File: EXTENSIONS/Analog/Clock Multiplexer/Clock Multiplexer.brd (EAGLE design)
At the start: 68 x 71 mm, 17 parts

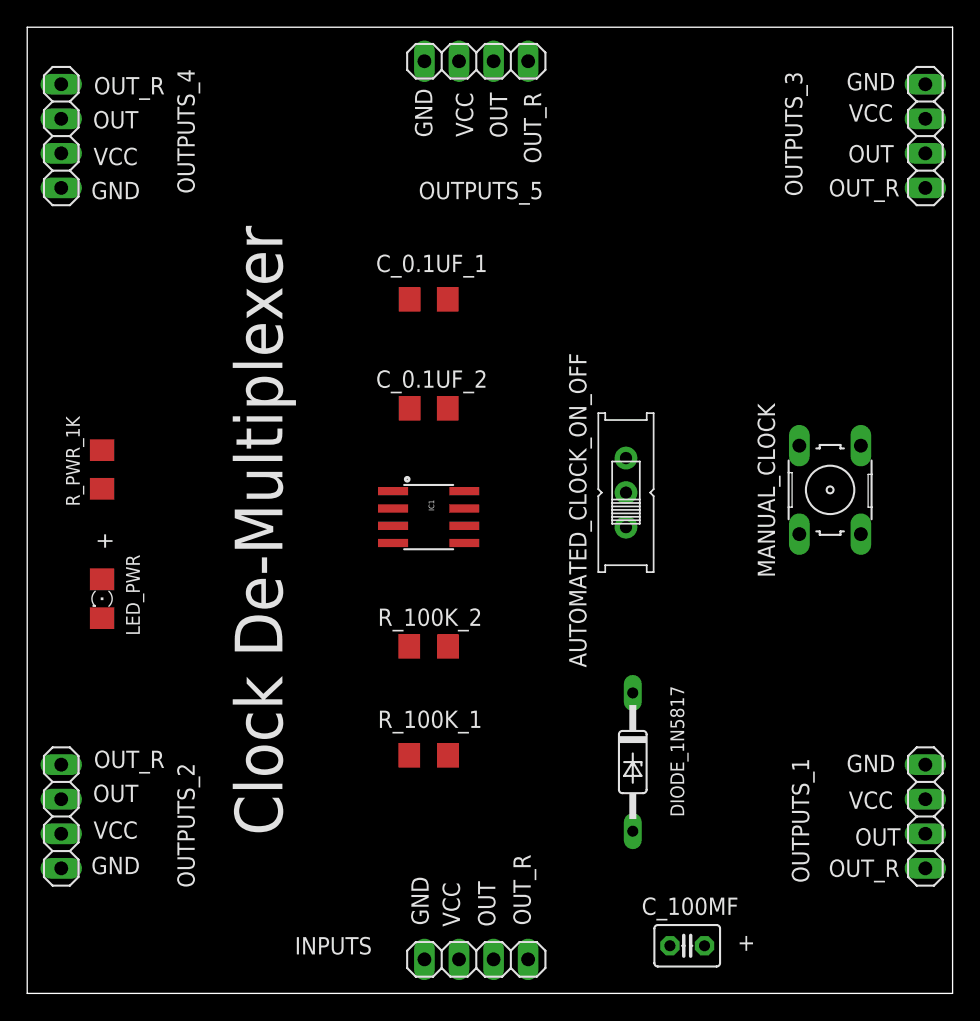
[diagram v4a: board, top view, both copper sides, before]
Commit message: Create v2 of Clock de-multiplexer
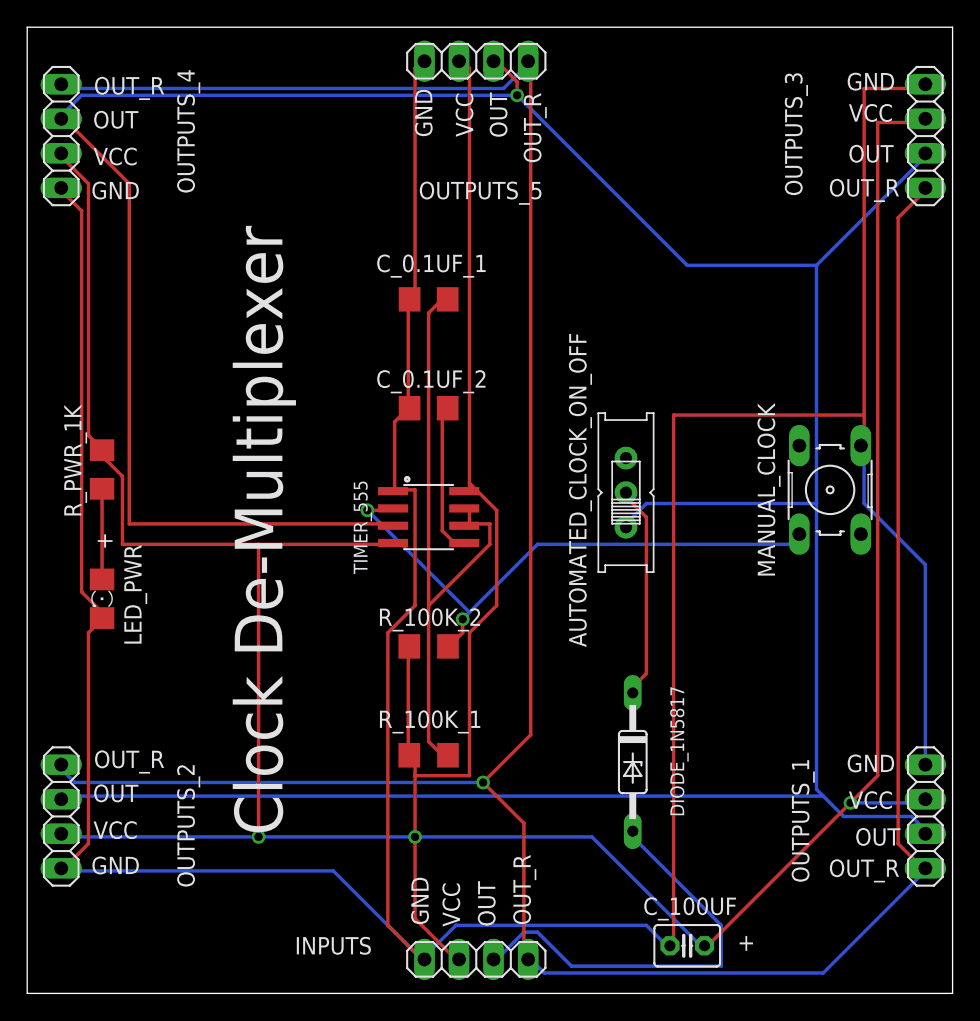
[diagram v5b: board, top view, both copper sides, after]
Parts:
- renumbered C_100MF to C_100UF, IC1 to TIMER_555
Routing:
- net GND: track 0.00 -> 283.3 mm
- net VCC: track 0.00 -> 282.8 mm, vias 0 -> 3
- net TMR555_OUTPUT_2: track 0.00 -> 247.2 mm, vias 0 -> 1
- net TMR555_OUTPUT_REVERSE: track 0.00 -> 221.7 mm, vias 0 -> 1
- net N$3: track 0.00 -> 46.3 mm
- net N$5: track 0.00 -> 42.3 mm, vias 0 -> 2
- net TMR555_OUTPUT: track 0.00 -> 31.2 mm
- net N$2: track 0.00 -> 15.8 mm
- net N$4: track 0.00 -> 11.5 mm
- net N$1: track 0.00 -> 6.66 mm

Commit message: Fix bug in clock multi plexer
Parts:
- removed DIODE_1N5817: 1N821, diode:DO35Z10
- added DIODE_1N5817_1, DIODE_1N5817_2: 1N821, diode:DO35Z10
- added R_TMR555_OUTPUT_2_PD_1K: (no value), adafruit:R1206
- moved AUTOMATED_CLOCK_ON_OFF 6.08 mm to (47.0, 54.8)
- moved LED_PWR 4.12 mm to (8.50, 37.0)
- moved MANUAL_CLOCK 3.00 mm to (58.0, 49.0)
- moved R_PWR_1K 3.00 mm to (7.50, 47.5)
- renumbered C_0.1UF_1 to C_10UF_1, R_100K_1 to R_10K_1, R_100K_2 to R_1K_2
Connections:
- new net TIMER_OUTPUT: DIODE_1N5817_2.A, TIMER_555.3
- net GND: now also R_TMR555_OUTPUT_2_PD_1K.2
- net N$2: now also DIODE_1N5817_1.C; no longer DIODE_1N5817.C
- net TMR555_OUTPUT: now also DIODE_1N5817_1.A; no longer DIODE_1N5817.A
- net TMR555_OUTPUT_2: now also DIODE_1N5817_2.C, R_TMR555_OUTPUT_2_PD_1K.1; no longer TIMER_555.3
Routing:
- net GND: track 283.3 -> 0.00 mm
- net VCC: track 282.8 -> 0.00 mm, vias 3 -> 0
- net TMR555_OUTPUT_2: track 247.2 -> 0.00 mm, vias 1 -> 0
- net TMR555_OUTPUT_REVERSE: track 221.7 -> 0.00 mm, vias 1 -> 0
- net N$3: track 46.3 -> 0.00 mm
- net N$5: track 42.3 -> 0.00 mm, vias 2 -> 0
- net TMR555_OUTPUT: track 31.2 -> 0.00 mm
- net N$2: track 15.8 -> 0.00 mm
- net N$4: track 11.5 -> 0.00 mm
- net N$1: track 6.66 -> 0.00 mm

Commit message: Update cheetah booster
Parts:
- moved DIODE_1N5817_2 39.6 mm to (7.00, 42.0)
- moved DIODE_1N5817_1 37.1 mm to (47.5, 65.0)
- moved LED_PWR 17.3 mm to (5.50, 54.0)
- moved R_PWR_1K 15.6 mm to (6.00, 63.0)
- moved AUTOMATED_CLOCK_ON_OFF 7.00 mm to (47.0, 47.8)
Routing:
- net GND: track 0.00 -> 272.3 mm, vias 0 -> 4
- net VCC: track 0.00 -> 248.9 mm, vias 0 -> 2
- net TMR555_OUTPUT_REVERSE: track 0.00 -> 217.5 mm, vias 0 -> 1
- net TMR555_OUTPUT_2: track 0.00 -> 196.3 mm, vias 0 -> 1
- net N$5: track 0.00 -> 59.0 mm
- net TMR555_OUTPUT: track 0.00 -> 50.1 mm
- net N$3: track 0.00 -> 39.1 mm
- net TIMER_OUTPUT: track 0.00 -> 25.9 mm
- net N$2: track 0.00 -> 23.6 mm
- net N$4: track 0.00 -> 11.3 mm
- net N$1: track 0.00 -> 6.39 mm
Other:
- board text added: "PCBv3 - 2020.02"
- board text removed: "PCBv2 - 2019.12"
